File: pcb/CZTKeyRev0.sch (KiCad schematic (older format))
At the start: 165 parts

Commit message: Layout done in PCB, idk done sum stuff
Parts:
- removed R?: R_Small, symbol Device:R_Small
- removed SW?: SW_Push, symbol Switch:SW_Push
- added ENC1: Rotary_Encoder_Switch, Rotary_Encoder:RotaryEncoder_Alps_EC11E-Switch_Vertical_H20mm, symbol Device:Rotary_Encoder_Switch
- added MX_SPACER_125: MX-NoLED, MX_Alps_Hybrid:MX-1.25U-NoLED, symbol MX_Alps_Hybrid:MX-NoLED
- added OLED1: SSD1306, SSD1306:128x64OLED, symbol SSD1306-128x64_OLED:SSD1306
- D1, D10, D11, D12, D13, D14, D15, D16, D17, D18, D19, D2, D20, D21, D22, D23, D24, D25, D26, D27, D28, D29, D3, D30, D31, D32, D33, D34, D35, D36, D37, D38, D39, D4, D40, D41, D42, D43, D44, D45, D46, D47, D48, D49, D5, D50, D51, D52, D53, D54, D55, D56, D57, D58, D59, D6, D60, D61, D62, D63, D64, D65, D66, D67, D68, D69, D7, D70, D71, D72, D73, D74, D75, D76, D77, D78, D79, D8, D80, D81, D9: renamed from D?; footprint (none) -> Diode_THT:D_DO-35_SOD27_P5.08mm_Vertical_KathodeUp
- MX_0, MX_1, MX_2, MX_3, MX_4, MX_5, MX_6, MX_7, MX_8, MX_9, MX_F1, MX_F10, MX_F11, MX_F12, MX_F2, MX_F3, MX_F4, MX_F5, MX_F6, MX_F7, MX_F8, MX_F9: footprint (none) -> MX_Alps_Hybrid:MX-1U-NoLED
- MX_A1: renamed from MX_A; footprint (none) -> MX_Alps_Hybrid:MX-1U-NoLED
- MX_ALT_L1: renamed from MX_ALT; footprint (none) -> MX_Alps_Hybrid:MX-1.25U-NoLED
- MX_ALT_R1: renamed from MX_ALT1; footprint (none) -> MX_Alps_Hybrid:MX-1.5U-NoLED
- MX_B1: renamed from MX_B; footprint (none) -> MX_Alps_Hybrid:MX-1U-NoLED
- MX_BACKSPACE1: renamed from MX_BACKSPACE; footprint (none) -> MX_Alps_Hybrid:MX-2U-NoLED
- MX_BCKSLASH1: renamed from MX_BCKSLASH; footprint (none) -> MX_Alps_Hybrid:MX-1.5U-NoLED
- MX_BR_L1: renamed from MX_BR2; footprint (none) -> MX_Alps_Hybrid:MX-1U-NoLED
- MX_BR_R1: renamed from MX_BR1; footprint (none) -> MX_Alps_Hybrid:MX-1U-NoLED
- MX_C1: renamed from MX_C; footprint (none) -> MX_Alps_Hybrid:MX-1U-NoLED
- MX_CAPS1: renamed from MX_CAPS; footprint (none) -> MX_Alps_Hybrid:MX-1.75U-NoLED
- MX_COMMA1: renamed from MX_COMMA; footprint (none) -> MX_Alps_Hybrid:MX-1U-NoLED
- MX_CTRL_L1: renamed from MX_CTRL; footprint (none) -> MX_Alps_Hybrid:MX-1.25U-NoLED
- MX_CTRL_R1: renamed from MX_CTRL1; footprint (none) -> MX_Alps_Hybrid:MX-1.5U-NoLED
- MX_D1: renamed from MX_D; footprint (none) -> MX_Alps_Hybrid:MX-1U-NoLED
- MX_DELETE1: renamed from MX_DELETE; footprint (none) -> MX_Alps_Hybrid:MX-1U-NoLED
- MX_DOT1: renamed from MX_DOT; footprint (none) -> MX_Alps_Hybrid:MX-1U-NoLED
- MX_DOWN1: renamed from MX_DOWN; footprint (none) -> MX_Alps_Hybrid:MX-1U-NoLED
- MX_E1: renamed from MX_E; footprint (none) -> MX_Alps_Hybrid:MX-1U-NoLED
- MX_ENTER1: renamed from MX_ENTER; footprint (none) -> MX_Alps_Hybrid:MX-2.25U-NoLED
- MX_EQUAL1: renamed from MX_EQUAL; footprint (none) -> MX_Alps_Hybrid:MX-1U-NoLED
- MX_ESC1: renamed from MX_ESC; footprint (none) -> MX_Alps_Hybrid:MX-1U-NoLED
- MX_F13: renamed from MX_F; footprint (none) -> MX_Alps_Hybrid:MX-1U-NoLED
- MX_G1: renamed from MX_G; footprint (none) -> MX_Alps_Hybrid:MX-1U-NoLED
- MX_H1: renamed from MX_H; footprint (none) -> MX_Alps_Hybrid:MX-1U-NoLED
- MX_I1: renamed from MX_I; footprint (none) -> MX_Alps_Hybrid:MX-1U-NoLED
- MX_INSERT1: renamed from MX_INSERT; footprint (none) -> MX_Alps_Hybrid:MX-1U-NoLED
- MX_J1: renamed from MX_J; footprint (none) -> MX_Alps_Hybrid:MX-1U-NoLED
- MX_K1: renamed from MX_K; footprint (none) -> MX_Alps_Hybrid:MX-1U-NoLED
- MX_L1: renamed from MX_L; footprint (none) -> MX_Alps_Hybrid:MX-1U-NoLED
- MX_LEFT1: renamed from MX_LEFT; footprint (none) -> MX_Alps_Hybrid:MX-1U-NoLED
- MX_M1: renamed from MX_M; footprint (none) -> MX_Alps_Hybrid:MX-1U-NoLED
- MX_MINUS1: renamed from MX_MINUS; footprint (none) -> MX_Alps_Hybrid:MX-1U-NoLED
- MX_N1: renamed from MX_N; footprint (none) -> MX_Alps_Hybrid:MX-1U-NoLED
- MX_O1: renamed from MX_O; footprint (none) -> MX_Alps_Hybrid:MX-1U-NoLED
- MX_P1: renamed from MX_P; footprint (none) -> MX_Alps_Hybrid:MX-1U-NoLED
- MX_PGDWN1: renamed from MX_PGDWN; footprint (none) -> MX_Alps_Hybrid:MX-1U-NoLED
- MX_PGUP1: renamed from MX_PGUP; footprint (none) -> MX_Alps_Hybrid:MX-1U-NoLED
- MX_PRTSC1: renamed from MX_PRTSC; footprint (none) -> MX_Alps_Hybrid:MX-1U-NoLED
- MX_Q1: renamed from MX_Q; footprint (none) -> MX_Alps_Hybrid:MX-1U-NoLED
- MX_QUOTE1: renamed from MX_QUOTE; footprint (none) -> MX_Alps_Hybrid:MX-1U-NoLED
- MX_R1: renamed from MX_R; footprint (none) -> MX_Alps_Hybrid:MX-1U-NoLED
- MX_RIGHT1: renamed from MX_RIGHT; footprint (none) -> MX_Alps_Hybrid:MX-1U-NoLED
- MX_S1: renamed from MX_S; footprint (none) -> MX_Alps_Hybrid:MX-1U-NoLED
- MX_SEMIC1: renamed from MX_SEMIC; footprint (none) -> MX_Alps_Hybrid:MX-1U-NoLED
- MX_SHIFT_L1: renamed from MX_SHIFT; footprint (none) -> MX_Alps_Hybrid:MX-2.25U-NoLED
- MX_SHIFT_R1: renamed from MX_SHIFT1; footprint (none) -> MX_Alps_Hybrid:MX-1.75U-NoLED
- MX_SLASH1: renamed from MX_SLASH; footprint (none) -> MX_Alps_Hybrid:MX-1U-NoLED
- MX_SPACE1: renamed from MX_SPACE; footprint (none) -> MX_Alps_Hybrid:MX-6.25U-NoLED
- MX_T1: renamed from MX_T; footprint (none) -> MX_Alps_Hybrid:MX-1U-NoLED
- MX_TAB1: renamed from MX_TAB; footprint (none) -> MX_Alps_Hybrid:MX-1.5U-NoLED
- MX_TILDE1: renamed from MX_TILDE; footprint (none) -> MX_Alps_Hybrid:MX-1U-NoLED
- MX_U1: renamed from MX_U; footprint (none) -> MX_Alps_Hybrid:MX-1U-NoLED
- MX_UP1: renamed from MX_UP; footprint (none) -> MX_Alps_Hybrid:MX-1U-NoLED
- MX_V1: renamed from MX_V; footprint (none) -> MX_Alps_Hybrid:MX-1U-NoLED
- MX_W1: renamed from MX_W; footprint (none) -> MX_Alps_Hybrid:MX-1U-NoLED
- MX_WIN1: renamed from MX_WIN; footprint (none) -> MX_Alps_Hybrid:MX-1.25U-NoLED
- MX_X1: renamed from MX_X; footprint (none) -> MX_Alps_Hybrid:MX-1U-NoLED
- MX_Y1: renamed from MX_Y; footprint (none) -> MX_Alps_Hybrid:MX-1U-NoLED
- MX_Z1: renamed from MX_Z; footprint (none) -> MX_Alps_Hybrid:MX-1U-NoLED
- U1: renamed from U?; footprint (none) -> proton_c:proton_c
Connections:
- net labels removed: RESET
- wire segments 254 -> 249
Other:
- moved on the sheet: D1, D10, D11, D12, D13, D14, D15, D16, D17, D18, D19, D2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

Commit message: Edits to layout and sutff
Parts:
- added C1, C2: 100n, symbol Device:C_Small
- added D? (x5): D_Small, Diode_THT:D_DO-35_SOD27_P5.08mm_Vertical_KathodeUp, symbol Device:D_Small
- added MX_MAC: MX-NoLED, MX_Alps_Hybrid:MX-1.25U-NoLED, symbol MX_Alps_Hybrid:MX-NoLED
- added MX_MAC, MX_MAC?: MX-NoLED, MX_Alps_Hybrid:MX-1.75U-NoLED, symbol MX_Alps_Hybrid:MX-NoLED
- added MX_MAC: MX-NoLED, MX_Alps_Hybrid:MX-1.5U-NoLED, symbol MX_Alps_Hybrid:MX-NoLED
- added MX_MAC: MX-NoLED, MX_Alps_Hybrid:MX-1U-NoLED, symbol MX_Alps_Hybrid:MX-NoLED
- added R1, R2: 10k, symbol Device:R_Small
- added R3, R4, R5: 10K, symbol Device:R_Small
- renumbered MX_F13 to MX_F0
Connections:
- net COL16 is gone; now on net COL15: MX_DELETE1.1 (COL), MX_INSERT1.1 (COL), MX_PGDWN1.1 (COL), MX_PGUP1.1 (COL)
- net +5V: now also ENC1.C, OLED1.2 (VCC), C1.2, C2.2, R5.1
- net COL0: now also MX_MAC.1 (COL), MX_MAC.1 (COL), MX_MAC.1 (COL), MX_MAC.1 (COL), MX_MAC?.1 (COL); no longer MX_CAPS1.1 (COL), MX_CTRL_L1.1 (COL), MX_ESC1.1 (COL), MX_TAB1.1 (COL), MX_TILDE1.1 (COL)
- net COL1: now also MX_CAPS1.1 (COL), MX_CTRL_L1.1 (COL), MX_ESC1.1 (COL), MX_TAB1.1 (COL), MX_TILDE1.1 (COL); no longer MX_1.1 (COL), MX_F1.1 (COL), MX_WIN1.1 (COL)
- net COL10: now also MX_9.1 (COL); no longer MX_0.1 (COL)
- net COL11: now also MX_0.1 (COL), MX_CTRL_R1.1 (COL); no longer MX_MINUS1.1 (COL)
- net COL12: now also MX_LEFT1.1 (COL), MX_MINUS1.1 (COL), MX_SHIFT_R1.1 (COL); no longer MX_CTRL_R1.1 (COL), MX_EQUAL1.1 (COL)
- net COL13: now also MX_DOWN1.1 (COL), MX_EQUAL1.1 (COL); no longer MX_LEFT1.1 (COL), MX_SHIFT_R1.1 (COL)
- net COL14: no longer MX_DOWN1.1 (COL)
- net COL2: now also MX_1.1 (COL), MX_F1.1 (COL), MX_WIN1.1 (COL); no longer MX_2.1 (COL), MX_F2.1 (COL)
- net COL3: now also MX_2.1 (COL), MX_F2.1 (COL); no longer MX_3.1 (COL), MX_F3.1 (COL)
- net COL4: now also MX_3.1 (COL), MX_F3.1 (COL); no longer MX_4.1 (COL), MX_F4.1 (COL)
- net COL5: now also MX_4.1 (COL), MX_F4.1 (COL); no longer MX_5.1 (COL)
- net COL6: now also MX_5.1 (COL); no longer MX_6.1 (COL)
- net COL7: now also MX_6.1 (COL); no longer MX_7.1 (COL)
- net COL8: now also MX_7.1 (COL); no longer MX_8.1 (COL)
- net COL9: now also MX_8.1 (COL); no longer MX_9.1 (COL)
- net ROW1: now also D?.1 (K)
- net ROW2: now also D?.1 (K)
- net ROW3: now also D?.1 (K)
- net ROW4: now also D?.1 (K)
- net ROW5: now also D?.1 (K)
- net VCC: now also ENC1.S1, OLED1.1 (GND), R1.1, R2.1
- net OLEDSCL: now reaches U1.B6 (PB6/SCL)
- net OLEDSCL: now also OLED1.3 (SCL)
- net OLEDSDA: now reaches U1.B7 (PB7/SDA)
- net OLEDSDA: now also OLED1.4 (SDA)
- net at ENC1.A: now also R1.2, R3.1
- net at ENC1.B: now also R2.2, R4.1
- net ENC_SW: now reaches ENC1.S2
- net ENC_SW: now also R5.2
- new net: D?.2 (A), MX_MAC.2 (ROW) (x4)
- new net: D?.2 (A), MX_MAC?.2 (ROW)
- new net ENC_A: C2.1, R3.2
- new net ENC_B: C1.1, R4.2
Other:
- moved on the sheet: D1, D10, D11, D12, D13, D14, D15, D16, D17, D18, D19, D2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

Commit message: WS2812B Matrix
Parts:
- added D? (x87): WS2812B, LED_SMD:LED_WS2812B_PLCC4_5.0x5.0mm_P3.2mm, symbol LED:WS2812B
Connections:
- net +5V: now also D?.1 (VDD), D?.1 (VDD), D?.1 (VDD), D?.1 (VDD), D?.1 (VDD), D?.1 (VDD), D?.1 (VDD), D?.1 (VDD), D?.1 (VDD), D?.1 (VDD), D?.1 (VDD), D?.1 (VDD), D?.1 (VDD), D?.1 (VDD), D?.1 (VDD), D?.1 (VDD), D?.1 (VDD), D?.1 (VDD), D?.1 (VDD), D?.1 (VDD), D?.1 (VDD), D?.1 (VDD), D?.1 (VDD), D?.1 (VDD), D?.1 (VDD), D?.1 (VDD), D?.1 (VDD), D?.1 (VDD), D?.1 (VDD), D?.1 (VDD), D?.1 (VDD), D?.1 (VDD), D?.1 (VDD), D?.1 (VDD), D?.1 (VDD), D?.1 (VDD), D?.1 (VDD), D?.1 (VDD), D?.1 (VDD), D?.1 (VDD), D?.1 (VDD), D?.1 (VDD), D?.1 (VDD), D?.1 (VDD), D?.1 (VDD), D?.1 (VDD), D?.1 (VDD), D?.1 (VDD), D?.1 (VDD), D?.1 (VDD), D?.1 (VDD), D?.1 (VDD), D?.1 (VDD), D?.1 (VDD), D?.1 (VDD), D?.1 (VDD), D?.1 (VDD), D?.1 (VDD), D?.1 (VDD), D?.1 (VDD), D?.1 (VDD), D?.1 (VDD), D?.1 (VDD), D?.1 (VDD), D?.1 (VDD), D?.1 (VDD), D?.1 (VDD), D?.1 (VDD), D?.1 (VDD), D?.1 (VDD), D?.1 (VDD), D?.1 (VDD), D?.1 (VDD), D?.1 (VDD), D?.1 (VDD), D?.1 (VDD), D?.1 (VDD), D?.1 (VDD), D?.1 (VDD), D?.1 (VDD), D?.1 (VDD), D?.1 (VDD), D?.1 (VDD), D?.1 (VDD), D?.1 (VDD), D?.1 (VDD), D?.1 (VDD), D?.3 (VSS), D?.3 (VSS), D?.3 (VSS), D?.3 (VSS), D?.3 (VSS), D?.3 (VSS), D?.3 (VSS), D?.3 (VSS), D?.3 (VSS), D?.3 (VSS), D?.3 (VSS), D?.3 (VSS), D?.3 (VSS), D?.3 (VSS), D?.3 (VSS), D?.3 (VSS), D?.3 (VSS), D?.3 (VSS), D?.3 (VSS), D?.3 (VSS), D?.3 (VSS), D?.3 (VSS), D?.3 (VSS), D?.3 (VSS), D?.3 (VSS), D?.3 (VSS), D?.3 (VSS), D?.3 (VSS), D?.3 (VSS), D?.3 (VSS), D?.3 (VSS), D?.3 (VSS), D?.3 (VSS), D?.3 (VSS), D?.3 (VSS), D?.3 (VSS), D?.3 (VSS), D?.3 (VSS), D?.3 (VSS), D?.3 (VSS), D?.3 (VSS), D?.3 (VSS), D?.3 (VSS), D?.3 (VSS), D?.3 (VSS), D?.3 (VSS), D?.3 (VSS), D?.3 (VSS), D?.3 (VSS), D?.3 (VSS), D?.3 (VSS), D?.3 (VSS), D?.3 (VSS), D?.3 (VSS), D?.3 (VSS), D?.3 (VSS), D?.3 (VSS), D?.3 (VSS), D?.3 (VSS), D?.3 (VSS), D?.3 (VSS), D?.3 (VSS), D?.3 (VSS), D?.3 (VSS), D?.3 (VSS), D?.3 (VSS), D?.3 (VSS), D?.3 (VSS), D?.3 (VSS), D?.3 (VSS), D?.3 (VSS), D?.3 (VSS), D?.3 (VSS), D?.3 (VSS), D?.3 (VSS), D?.3 (VSS), D?.3 (VSS), D?.3 (VSS), D?.3 (VSS), D?.3 (VSS), D?.3 (VSS), D?.3 (VSS), D?.3 (VSS), D?.3 (VSS), D?.3 (VSS), D?.3 (VSS), D?.3 (VSS)
- net RGB_MATRIX: now reaches U1.LED
- net RGB_MATRIX: now also D?.4 (DIN)
- new net: D?.2 (DOUT), D?.4 (DIN) (x81)
- new net D_ROW2: D?.2 (DOUT), D?.4 (DIN)
- new net D_ROW3: D?.2 (DOUT), D?.4 (DIN)
- new net D_ROW4: D?.2 (DOUT), D?.4 (DIN)
- new net D_ROW5: D?.2 (DOUT), D?.4 (DIN)
- new net D_ROW6: D?.2 (DOUT), D?.4 (DIN)
- no-connect marks 0 -> 1

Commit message: Wired up matrix and renamed WS2812B from D? to WS?
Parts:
- gave numbers to parts that had none: 1

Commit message: Positioned things
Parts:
- removed WS: WS2812B, LED_SMD:LED_WS2812B_PLCC4_5.0x5.0mm_P3.2mm, symbol LED:WS2812B
- C1, C2: footprint (none) -> Capacitor_SMD:C_0603_1608Metric
- MX_MAC2: renamed from MX_MAC; footprint MX_Alps_Hybrid:MX-1.5U-NoLED -> MX_Alps_Hybrid:MX-1U-NoLED
- MX_MAC3: renamed from MX_MAC; footprint MX_Alps_Hybrid:MX-1.75U-NoLED -> MX_Alps_Hybrid:MX-1U-NoLED
- MX_MAC4: renamed from MX_MAC?; footprint MX_Alps_Hybrid:MX-1.75U-NoLED -> MX_Alps_Hybrid:MX-1U-NoLED
- MX_MAC5: renamed from MX_MAC; footprint MX_Alps_Hybrid:MX-1.25U-NoLED -> MX_Alps_Hybrid:MX-1U-NoLED
- R1, R2, R3, R4: footprint (none) -> Resistor_SMD:R_Array_Convex_4x0603
- R5: footprint (none) -> Resistor_SMD:R_0603_1608Metric
- WS1, WS10, WS11, WS12, WS13, WS14, WS15, WS16, WS17, WS18, WS19, WS2, WS20, WS21, WS22, WS23, WS24, WS25, WS26, WS27, WS28, WS29, WS3, WS30, WS31, WS32, WS33, WS34, WS35, WS36, WS37, WS38, WS39, WS4, WS40, WS41, WS42, WS43, WS44, WS45, WS46, WS47, WS48, WS49, WS5, WS50, WS51, WS52, WS53, WS54, WS55, WS56, WS57, WS58, WS59, WS6, WS60, WS61, WS62, WS63, WS64, WS65, WS66, WS67, WS68, WS69, WS7, WS70, WS71, WS72, WS73, WS74, WS75, WS76, WS77, WS78, WS79, WS8, WS80, WS81, WS82, WS83, WS84, WS85, WS86, WS9: renamed from WS; footprint LED_SMD:LED_WS2812B_PLCC4_5.0x5.0mm_P3.2mm -> WS2812B-edited:Neopixel_easy_LED_WS2812B_PLCC4_5.0x5.0mm_P3.2mm
- gave numbers to parts that had none: 5
- renumbered MX_MAC to MX_MAC1
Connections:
- net +5V: no longer C1.2, C2.2, OLED1.2 (VCC), R5.1, WS1.3 (VSS), WS10.3 (VSS), WS11.3 (VSS), WS12.3 (VSS), WS13.3 (VSS), WS14.3 (VSS), WS15.3 (VSS), WS16.3 (VSS), WS17.3 (VSS), WS18.3 (VSS), WS19.3 (VSS), WS2.3 (VSS), WS20.3 (VSS), WS21.3 (VSS), WS22.3 (VSS), WS23.3 (VSS), WS24.3 (VSS), WS25.3 (VSS), WS26.3 (VSS), WS27.3 (VSS), WS28.3 (VSS), WS29.3 (VSS), WS3.3 (VSS), WS30.3 (VSS), WS31.3 (VSS), WS32.3 (VSS), WS33.3 (VSS), WS34.3 (VSS), WS35.3 (VSS), WS36.3 (VSS), WS37.3 (VSS), WS38.3 (VSS), WS39.3 (VSS), WS4.3 (VSS), WS40.3 (VSS), WS41.3 (VSS), WS42.3 (VSS), WS43.3 (VSS), WS44.3 (VSS), WS45.3 (VSS), WS46.3 (VSS), WS47.3 (VSS), WS48.3 (VSS), WS49.3 (VSS), WS5.3 (VSS), WS50.3 (VSS), WS51.3 (VSS), WS52.3 (VSS), WS53.3 (VSS), WS54.3 (VSS), WS55.3 (VSS), WS56.3 (VSS), WS57.3 (VSS), WS58.3 (VSS), WS59.3 (VSS), WS6.3 (VSS), WS60.3 (VSS), WS61.3 (VSS), WS62.3 (VSS), WS63.3 (VSS), WS64.3 (VSS), WS65.3 (VSS), WS66.3 (VSS), WS67.3 (VSS), WS68.3 (VSS), WS69.3 (VSS), WS7.3 (VSS), WS70.3 (VSS), WS71.3 (VSS), WS72.3 (VSS), WS73.3 (VSS), WS74.3 (VSS), WS75.3 (VSS), WS76.3 (VSS), WS77.3 (VSS), WS78.3 (VSS), WS79.3 (VSS), WS8.3 (VSS), WS80.3 (VSS), WS81.3 (VSS), WS82.3 (VSS), WS83.3 (VSS), WS84.3 (VSS), WS85.3 (VSS), WS86.3 (VSS), WS9.3 (VSS)
- net ENC_A: now also U1.B11 (PB11)
- net ENC_B: now also U1.B12 (PB12)
- net ENC_SW: now also U1.B10 (PB10)
- net GND: now also C1.2, C2.2, OLED1.1 (GND), R5.1, WS1.3 (VSS), WS10.3 (VSS), WS11.3 (VSS), WS12.3 (VSS), WS13.3 (VSS), WS14.3 (VSS), WS15.3 (VSS), WS16.3 (VSS), WS17.3 (VSS), WS18.3 (VSS), WS19.3 (VSS), WS2.3 (VSS), WS20.3 (VSS), WS21.3 (VSS), WS22.3 (VSS), WS23.3 (VSS), WS24.3 (VSS), WS25.3 (VSS), WS26.3 (VSS), WS27.3 (VSS), WS28.3 (VSS), WS29.3 (VSS), WS3.3 (VSS), WS30.3 (VSS), WS31.3 (VSS), WS32.3 (VSS), WS33.3 (VSS), WS34.3 (VSS), WS35.3 (VSS), WS36.3 (VSS), WS37.3 (VSS), WS38.3 (VSS), WS39.3 (VSS), WS4.3 (VSS), WS40.3 (VSS), WS41.3 (VSS), WS42.3 (VSS), WS43.3 (VSS), WS44.3 (VSS), WS45.3 (VSS), WS46.3 (VSS), WS47.3 (VSS), WS48.3 (VSS), WS49.3 (VSS), WS5.3 (VSS), WS50.3 (VSS), WS51.3 (VSS), WS52.3 (VSS), WS53.3 (VSS), WS54.3 (VSS), WS55.3 (VSS), WS56.3 (VSS), WS57.3 (VSS), WS58.3 (VSS), WS59.3 (VSS), WS6.3 (VSS), WS60.3 (VSS), WS61.3 (VSS), WS62.3 (VSS), WS63.3 (VSS), WS64.3 (VSS), WS65.3 (VSS), WS66.3 (VSS), WS67.3 (VSS), WS68.3 (VSS), WS69.3 (VSS), WS7.3 (VSS), WS70.3 (VSS), WS71.3 (VSS), WS72.3 (VSS), WS73.3 (VSS), WS74.3 (VSS), WS75.3 (VSS), WS76.3 (VSS), WS77.3 (VSS), WS78.3 (VSS), WS79.3 (VSS), WS8.3 (VSS), WS80.3 (VSS), WS81.3 (VSS), WS82.3 (VSS), WS83.3 (VSS), WS84.3 (VSS), WS85.3 (VSS), WS86.3 (VSS), WS9.3 (VSS)
- net VCC: now also OLED1.2 (VCC); no longer OLED1.1 (GND)
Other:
- note added: "R1-5 i C1/2 budou SMD, stejný jako v Hub16, použiju JLCPCB assembly -> R1-4 je C107374, R5 je C144116 a C1 a 2 je C1591"

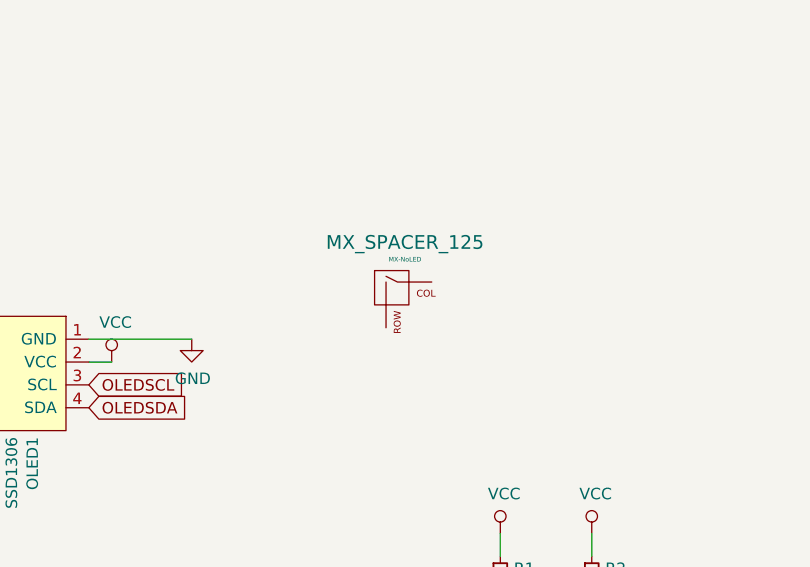
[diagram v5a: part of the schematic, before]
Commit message: Removed 1.25U spacer
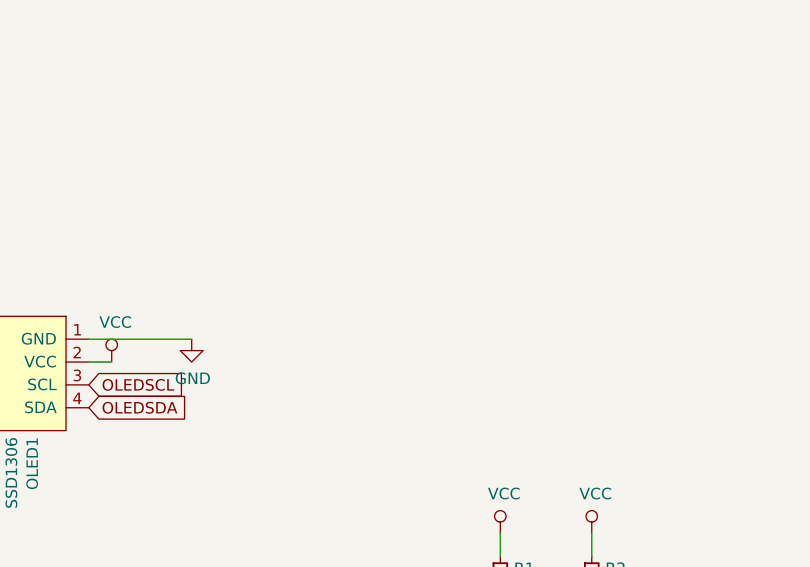
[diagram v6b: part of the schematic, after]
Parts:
- removed MX_SPACER_125: MX-NoLED, MX_Alps_Hybrid:MX-1.25U-NoLED, symbol MX_Alps_Hybrid:MX-NoLED
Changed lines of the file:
@@
-$EndComp
-$Comp
-L MX_Alps_Hybrid:MX-NoLED MX_SPACER_125
-U 1 1 5FD6D484
-P 5850 1450
-F 0 "MX_SPACER_125" H 5883 1673 60  0000 C CNN
-F 1 "MX-NoLED" H 5883 1599 20  0000 C CNN
-F 2 "MX_Alps_Hybrid:MX-1.25U-NoLED" H 5225 1425 60  0001 C CNN
-F 3 "" H 5225 1425 60  0001 C CNN
-	1    5850 1450
-	1    0    0    -1
 $EndComp
 $Comp

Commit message: Maybe final?
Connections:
- net COL0: now also U1.A2 (PA2)
- net COL1: now also U1.A1 (PA1)
- net COL10: now also U1.A6 (PA6)
- net COL11: now also U1.A7 (PA7)
- net COL12: now also U1.A8 (PA8)
- net COL13: now also U1.A15 (PA15)
- net COL14: now also U1.A14 (PA14/SWCLK)
- net COL15: now also U1.A13 (PA13/SWDIO)
- net COL2: now also U1.A0 (PA0)
- net COL3: now also U1.B8 (PB8)
- net COL4: now also U1.B13 (PB13/SCLK)
- net COL5: now also U1.B14 (PB14/MISO)
- net COL6: now also U1.B15 (PB15/MOSI)
- net COL7: now also U1.B9 (PB9)
- net COL8: now also U1.A4 (PA4/SPEAKER1)
- net COL9: now also U1.A5 (PA5/SPEAKER2)
- net ROW0: now also U1.B0 (PB0)
- net ROW1: now also U1.B1 (PB1)
- net ROW2: now also U1.B2 (PB2)
- net ROW3: now also U1.B3 (PB3)
- net ROW4: now also U1.B4 (PB4)
- net ROW5: now also U1.B5 (PB5)
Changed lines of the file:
@@
 Text GLabel 3250 2950 2    50   Input ~ 0
 ENC_SW
+Text GLabel 1200 2050 0    50   Input ~ 0
+ROW1
+Text GLabel 1200 2150 0    50   Input ~ 0
+ROW0
+Text GLabel 1200 1950 0    50   Input ~ 0
+ROW2
+Text GLabel 1200 1850 0    50   Input ~ 0
+ROW3
+Text GLabel 1200 1750 0    50   Input ~ 0
+ROW4
+Text GLabel 1200 1650 0    50   Input ~ 0
+ROW5
+Text GLabel 3250 1750 2    50   Input ~ 0
+COL3
+Text GLabel 3250 1650 2    50   Input ~ 0
+COL2
+Text GLabel 3250 1550 2    50   Input ~ 0
+COL1
+Text GLabel 3250 1450 2    50   Input ~ 0
+COL0
+Text GLabel 3250 1850 2    50   Input ~ 0
+COL4
+Text GLabel 3250 1950 2    50   Input ~ 0
+COL5
+Text GLabel 3250 2050 2    50   Input ~ 0
+COL6
+Text GLabel 3250 2150 2    50   Input ~ 0
+COL7
+Text GLabel 1200 2950 0    50   Input ~ 0
+COL8
+Text GLabel 1200 3050 0    50   Input ~ 0
+COL9
+Text GLabel 1200 3150 0    50   Input ~ 0
+COL10
+Text GLabel 1200 3250 0    50   Input ~ 0
+COL11
+Text GLabel 1200 3350 0    50   Input ~ 0
+COL12
+Text GLabel 1200 3450 0    50   Input ~ 0
+COL13
+Text GLabel 3250 3250 2    50   Input ~ 0
+COL14
+Text GLabel 3250 3350 2    50   Input ~ 0
+COL15
 $EndSCHEMATC

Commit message: did some stuff
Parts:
- added WS87: WS2812B, WS2812B-edited:Neopixel_easy_LED_WS2812B_PLCC4_5.0x5.0mm_P3.2mm, symbol LED:WS2812B
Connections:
- net +5V: now also WS87.1 (VDD)
- net GND: now also WS87.3 (VSS)
- net at WS83.4 (DIN): now also WS87.2 (DOUT); no longer WS82.2 (DOUT)
- new net: WS82.2 (DOUT), WS87.4 (DIN)
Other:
- moved on the sheet: C1, C2, D1, D10, D11, D12, D13, D14, D15, D16, D17, D18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
